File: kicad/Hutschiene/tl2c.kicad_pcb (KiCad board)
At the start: 4 copper layers, 175.9 x 86.5 mm, 92 parts, among them IC101 ATTINY20-X, P101 12VDC, P102 RJ45, P103 CTL CONN, P104 TPI Header, P105 DRV CONN, P106 240VAC, P107 CTL PWR, P108 UG, P109 5VDC, P110 EG, P111 OG, P112 DRV PWR, P201 Mode_Bridge, P501 CONN_PIR_OG, P502 CONN_PIR_EG, P503 CONN_PIR_UG, Q301 IRLML2502, Q302 IRLML2502, Q303 IRLML2502, Q401 IRLML2502, Q402 IRLML2502, Q403 IRLML2502, SW101 TL3315NF160Q, U201 LF120ABDT-TR, U202 TPS70933

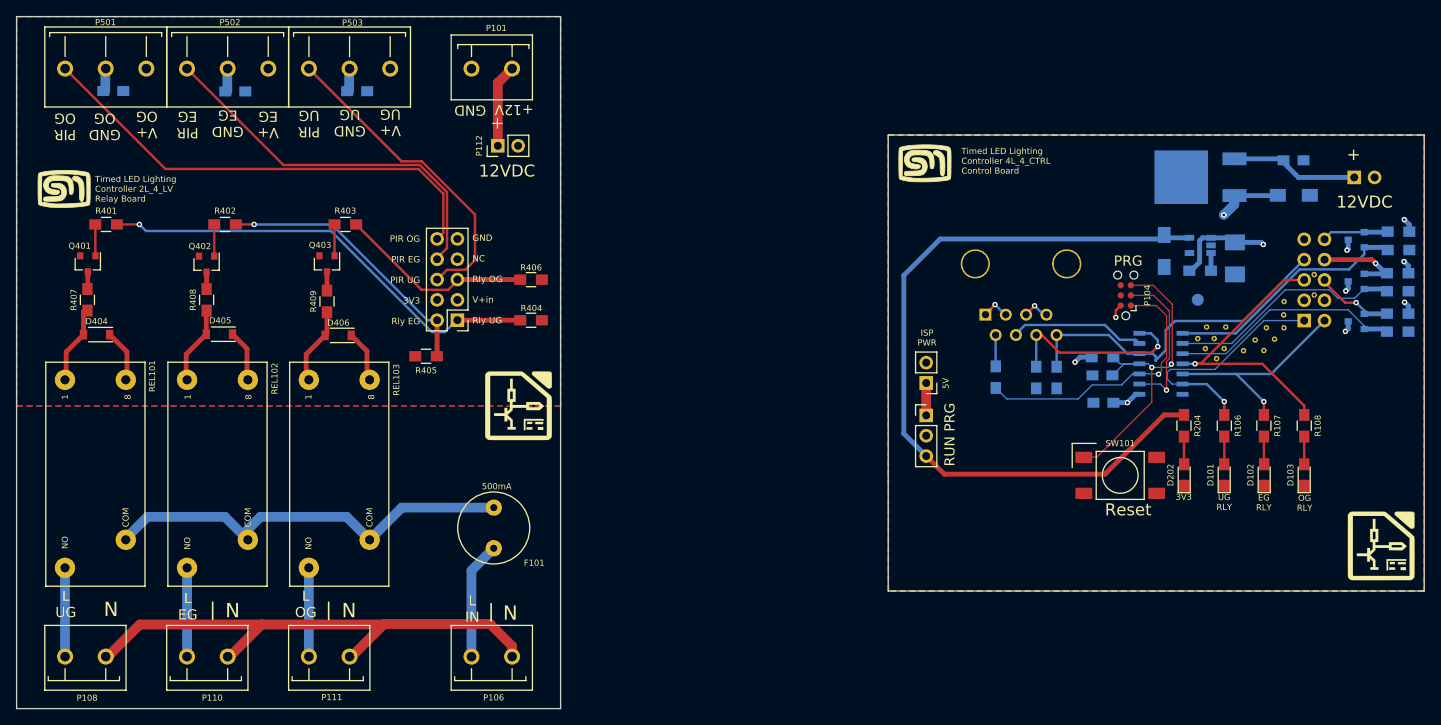
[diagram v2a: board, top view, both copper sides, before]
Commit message: In preperation for using a stencil - moved most 0805 back from handsolder to normal
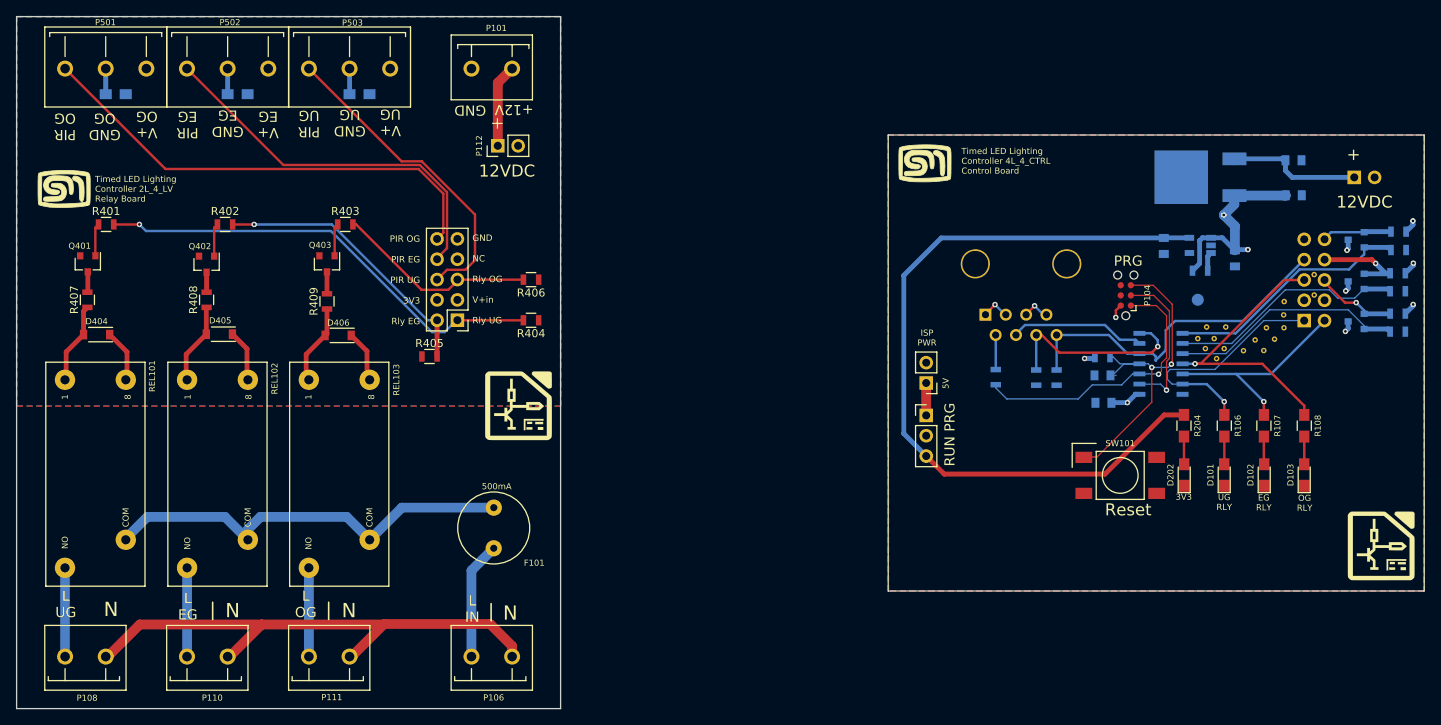
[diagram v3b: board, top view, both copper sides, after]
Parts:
- C101, C102, C201: footprint Capacitors_SMD:C_0805_HandSoldering -> Capacitors_SMD:C_0805
- C202: footprint Capacitors_SMD:C_1210_HandSoldering -> Capacitors_SMD:C_0805
- C203, C204: footprint Capacitors_SMD:C_1206_HandSoldering -> Capacitors_SMD:C_0805
- R101, R103, R104, R105, R202, R301, R302, R303, R307, R308, R309, R401, R402, R403, R404, R405, R406, R407, R408, R409: footprint Resistors_SMD:R_0805_HandSoldering -> Resistors_SMD:R_0805
- moved C204 0.63 mm to (189.2, 88.5)
- moved C501 0.50 mm to (58.1, 69.5)
- moved C502 0.48 mm to (88.6, 69.5)
- moved C503 0.45 mm to (73.4, 69.5)
- moved R405 0.43 mm to (97.4, 102.3)
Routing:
- net /PIR13/U+: track 26.5 -> 30.4 mm
- net GNDA: track 8.53 -> 9.78 mm
- net /PIR13/Ub+: track 11.8 -> 10.9 mm
- net /LED Driver/Relay_OG: track 25.0 -> 25.8 mm
- net /PIR13/PIR_EG: track 11.4 -> 12.2 mm
- net /LED Driver/Relay_UG: track 56.7 -> 57.5 mm

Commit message: Corrected issues with the connectors - Pushing to OSH Park
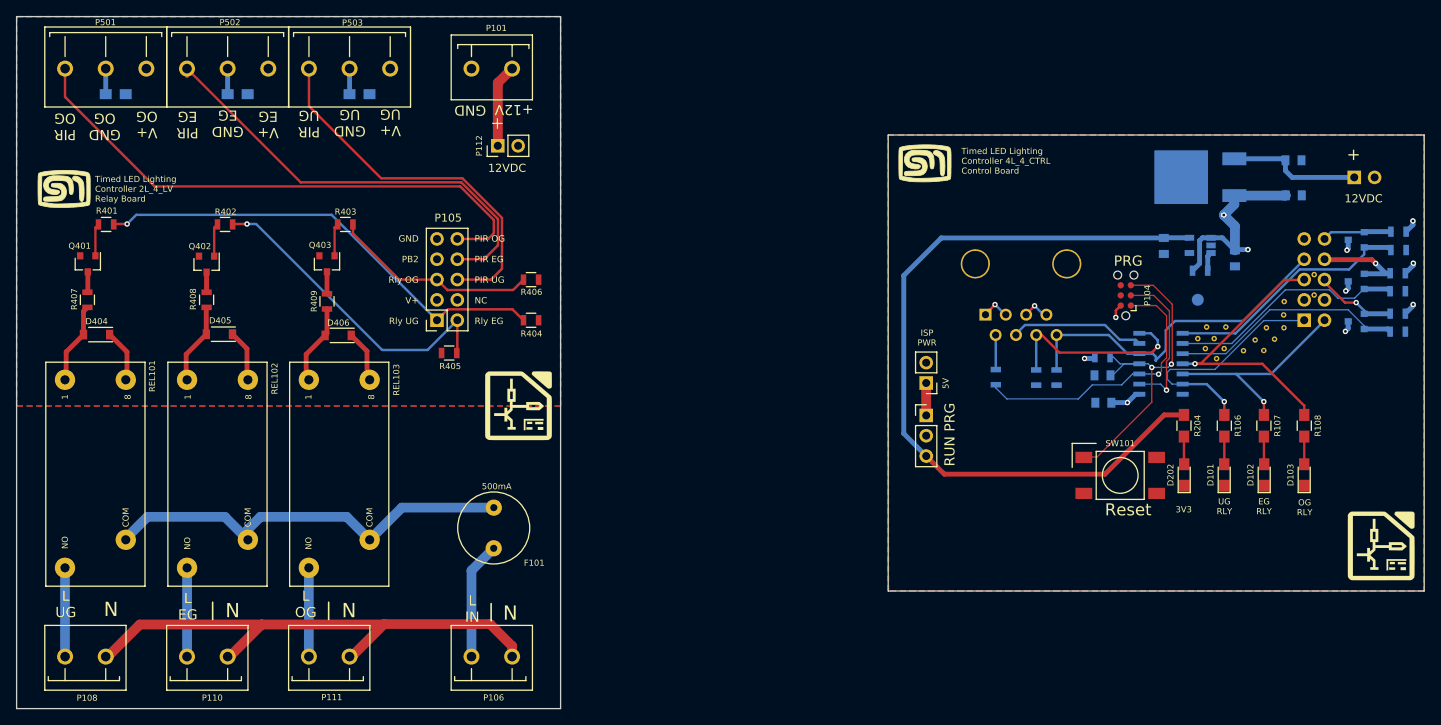
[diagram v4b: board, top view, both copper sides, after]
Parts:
- P105: footprint Pin_Headers:Pin_Header_Straight_2x05_Pitch2.54mm -> Socket_Strips:Socket_Strip_Straight_2x05_Pitch2.54mm
- moved P105 2.55 mm to (98.3, 97.8)
- moved R405 2.50 mm to (99.8, 101.9)
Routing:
- net /PIR_Connector/PIR_OG: track 59.7 -> 70.0 mm
- net /PIR_Connector/PIR_EG: track 47.8 -> 56.6 mm
- net /PIR_Connector/PIR_UG: track 40.0 -> 47.1 mm
- net /LED Driver/Relay_EG: track 35.0 -> 40.4 mm
- net /LED Driver/Relay_UG: track 57.5 -> 58.3 mm
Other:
- board text added: "GND PB2 Rly OG V+ Rly UG"
- board text added: "PIR OG PIR EG PIR UG NC Rly EG"
- board text removed: "GND NC Rly OG V+in Rly UG"
- board text removed: "PIR OG PIR EG PIR UG 3V3 Rly EG"
